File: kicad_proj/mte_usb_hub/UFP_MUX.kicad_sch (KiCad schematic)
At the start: 9 parts

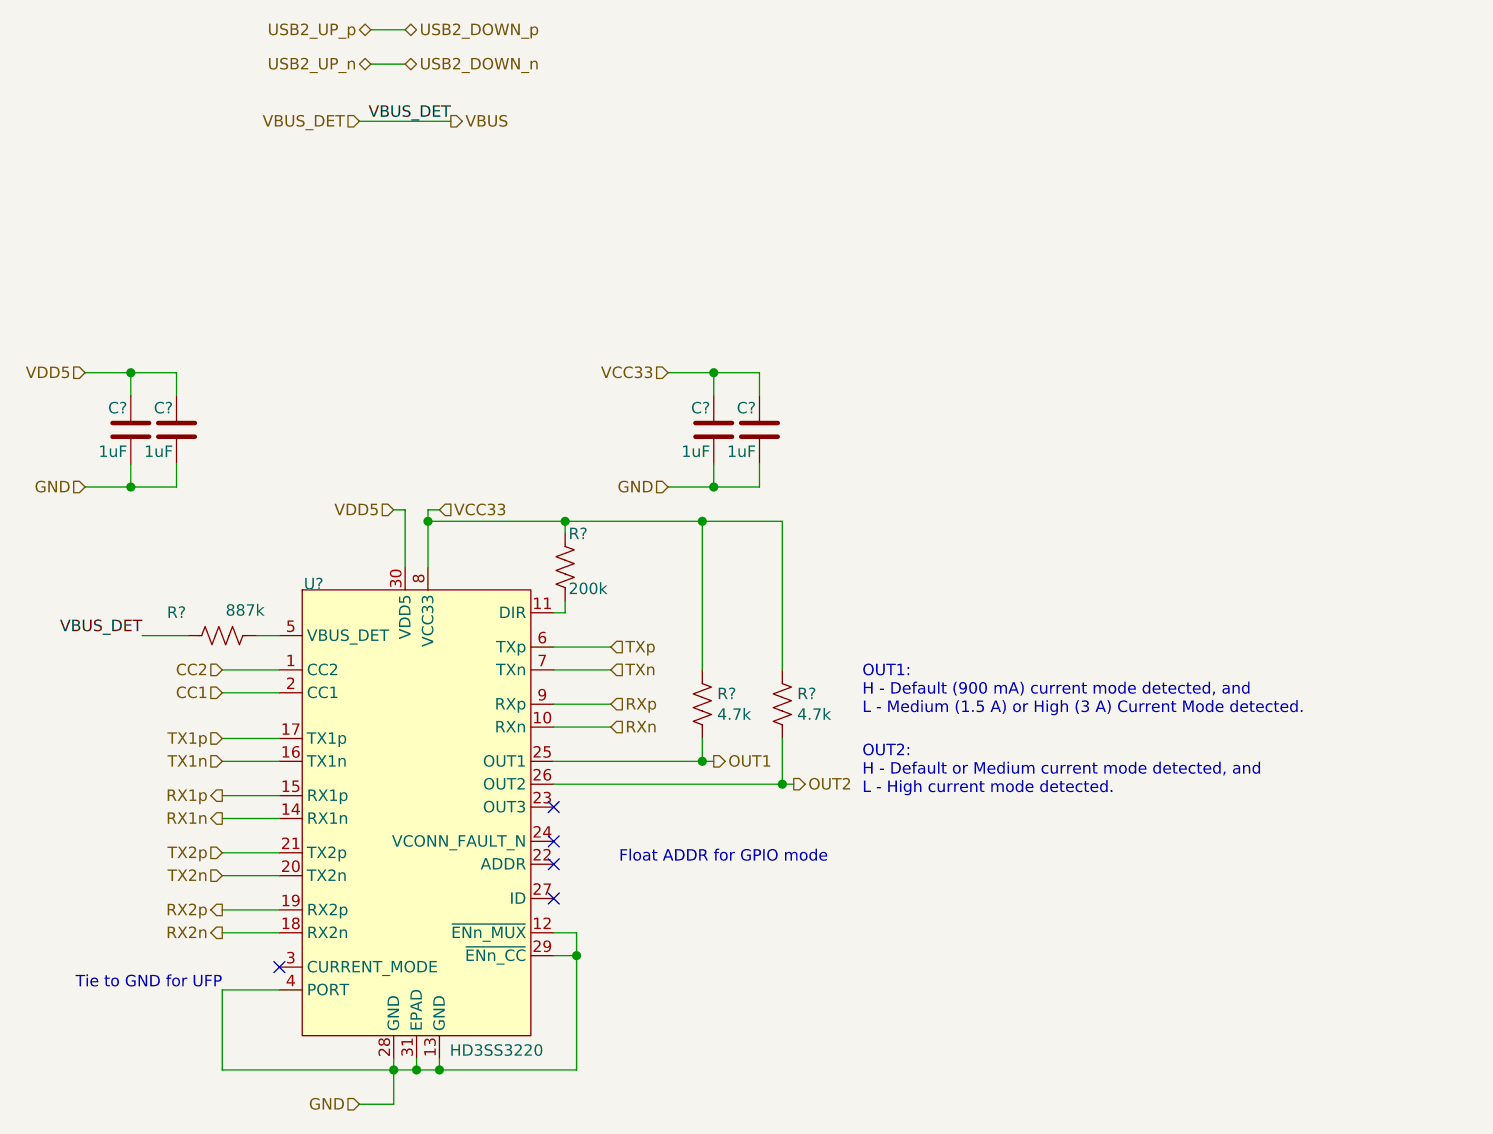
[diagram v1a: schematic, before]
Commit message: Updates input protection, output BC enabled
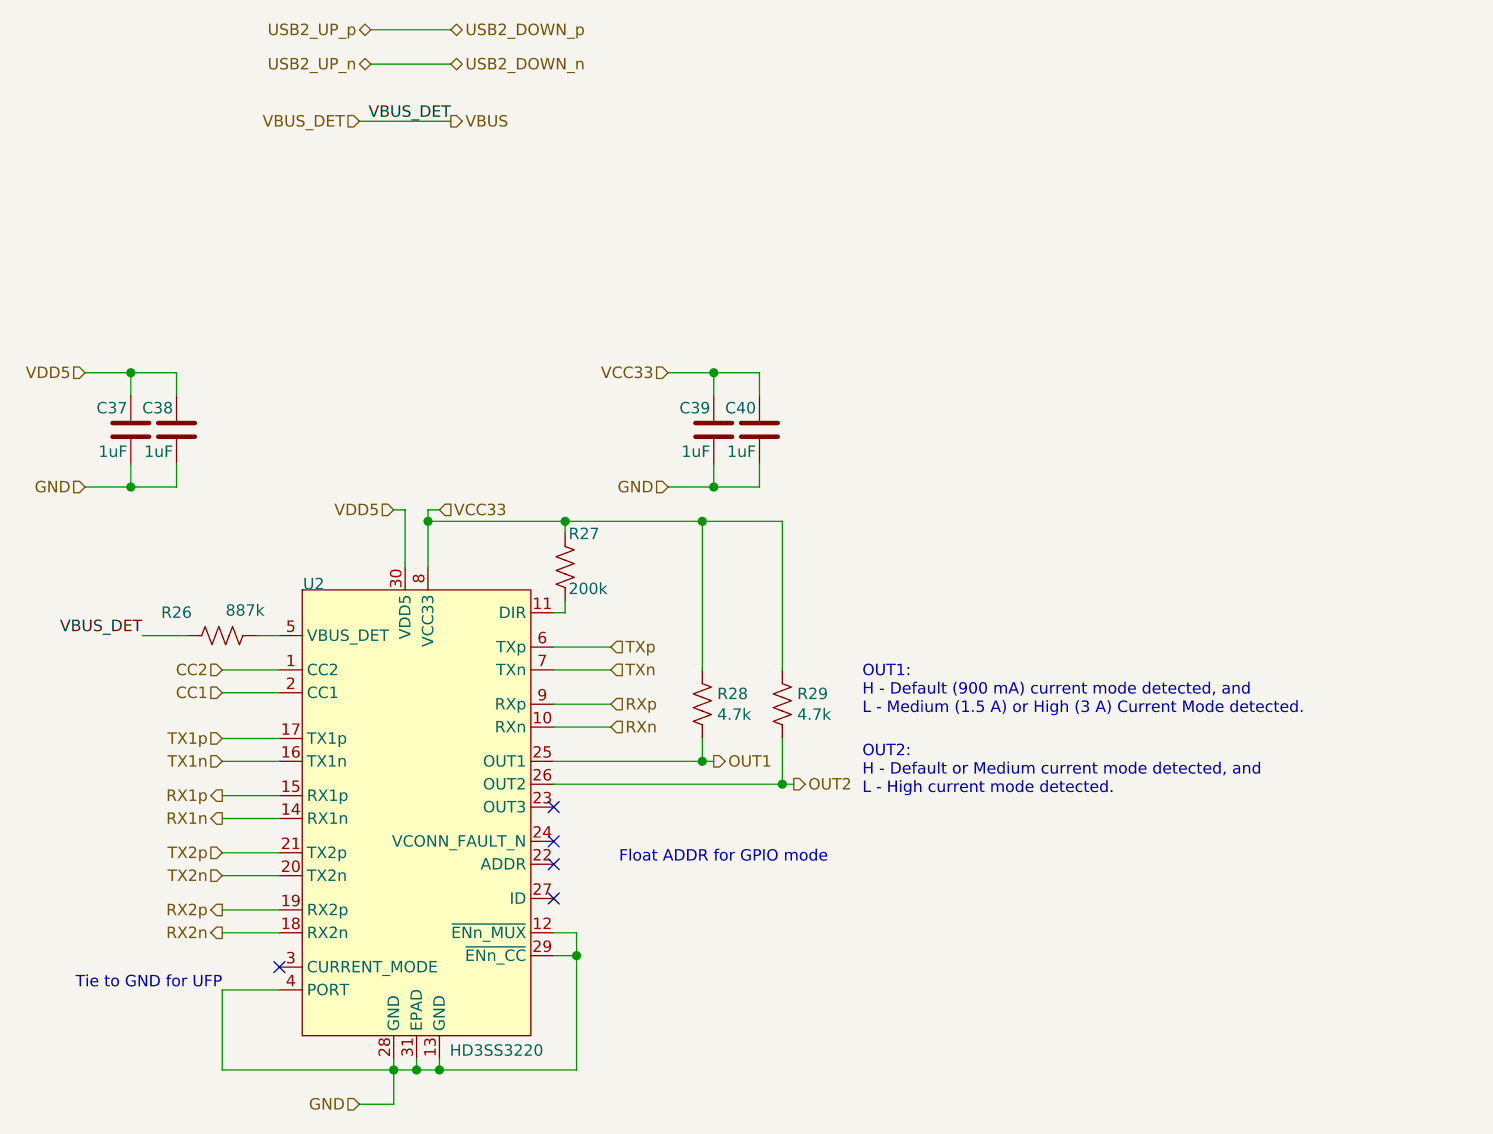
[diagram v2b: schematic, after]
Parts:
- gave numbers to parts that had none: 9
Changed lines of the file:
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@@
-(kicad_sch (version 20210126) (generator eeschema)
+(kicad_sch (version 20210406) (generator eeschema)
   (paper "A4")
   (junction (at 60.96 58.42) (diameter 1.016) (color 0 0 0 0))
@@
     (stroke (width 0) (type solid) (color 0 0 0 0))
   )
-  (wire (pts (xy 87.63 20.32) (xy 91.44 20.32))
-    (stroke (width 0) (type solid) (color 0 0 0 0))
-  )
-  (wire (pts (xy 87.63 24.13) (xy 91.44 24.13))
+  (wire (pts (xy 87.63 20.32) (xy 96.52 20.32))
+    (stroke (width 0) (type solid) (color 0 0 0 0))
+  )
+  (wire (pts (xy 87.63 24.13) (xy 96.52 24.13))
     (stroke (width 0) (type solid) (color 0 0 0 0))
   )
@@
     (effects (font (size 1.27 1.27)) (justify right))
   )
-  (hierarchical_label "USB2_DOWN_p" (shape bidirectional) (at 91.44 20.32 0)
-    (effects (font (size 1.27 1.27)) (justify left))
-  )
-  (hierarchical_label "USB2_DOWN_n" (shape bidirectional) (at 91.44 24.13 0)
-    (effects (font (size 1.27 1.27)) (justify left))
-  )
   (hierarchical_label "VCC33" (shape input) (at 95.25 73.66 0)
     (effects (font (size 1.27 1.27)) (justify left))
   )
+  (hierarchical_label "USB2_DOWN_p" (shape bidirectional) (at 96.52 20.32 0)
+    (effects (font (size 1.27 1.27)) (justify left))
+  )
+  (hierarchical_label "USB2_DOWN_n" (shape bidirectional) (at 96.52 24.13 0)
+    (effects (font (size 1.27 1.27)) (justify left))
+  )
   (hierarchical_label "VBUS" (shape output) (at 96.52 30.48 0)
     (effects (font (size 1.27 1.27)) (justify left))
@@
   (symbol (lib_id "mte_usb_hub:RC0402FR-07887KL") (at 71.12 87.63 90) (unit 1)
     (in_bom yes) (on_board yes)
-    (property "Reference" "R?" (id 0) (at 66.04 85.0708 90))
+    (property "Reference" "R26" (id 0) (at 66.04 85.0708 90))
     (property "Value" "RC0402FR-07887KL" (id 1) (at 71.12 90.17 90)
       (effects (font (size 1.27 1.27)) hide)
@@
   (symbol (lib_id "mte_usb_hub:RC0402JR-07200KL") (at 109.22 80.01 0) (unit 1)
     (in_bom yes) (on_board yes)
-    (property "Reference" "R?" (id 0) (at 109.6011 76.3206 0)
+    (property "Reference" "R27" (id 0) (at 109.6011 76.3206 0)
       (effects (font (size 1.27 1.27)) (justify left))
     )
@@
   (symbol (lib_id "mte_usb_hub:RC0402JR-074K7L") (at 124.46 95.25 0) (unit 1)
     (in_bom yes) (on_board yes)
-    (property "Reference" "R?" (id 0) (at 126.1111 94.1006 0)
+    (property "Reference" "R28" (id 0) (at 126.1111 94.1006 0)
       (effects (font (size 1.27 1.27)) (justify left))
     )
@@
   (symbol (lib_id "mte_usb_hub:RC0402JR-074K7L") (at 133.35 95.25 0) (unit 1)
     (in_bom yes) (on_board yes)
-    (property "Reference" "R?" (id 0) (at 135.0011 94.1006 0)
+    (property "Reference" "R29" (id 0) (at 135.0011 94.1006 0)
       (effects (font (size 1.27 1.27)) (justify left))
     )
@@
   (symbol (lib_id "mte_usb_hub:CC0402KRX5R7BB105") (at 60.96 64.77 0) (mirror y) (unit 1)
     (in_bom yes) (on_board yes)
-    (property "Reference" "C?" (id 0) (at 60.5789 62.3506 0)
+    (property "Reference" "C37" (id 0) (at 60.5789 62.3506 0)
       (effects (font (size 1.27 1.27)) (justify left))
     )
@@
   (symbol (lib_id "mte_usb_hub:CC0402KRX5R7BB105") (at 66.04 64.77 0) (mirror y) (unit 1)
     (in_bom yes) (on_board yes)
-    (property "Reference" "C?" (id 0) (at 65.6589 62.3506 0)
+    (property "Reference" "C38" (id 0) (at 65.6589 62.3506 0)
       (effects (font (size 1.27 1.27)) (justify left))
     )
@@
   (symbol (lib_id "mte_usb_hub:CC0402KRX5R7BB105") (at 125.73 64.77 0) (mirror y) (unit 1)
     (in_bom yes) (on_board yes)
-    (property "Reference" "C?" (id 0) (at 125.3489 62.3506 0)
+    (property "Reference" "C39" (id 0) (at 125.3489 62.3506 0)
       (effects (font (size 1.27 1.27)) (justify left))
     )
@@
   (symbol (lib_id "mte_usb_hub:CC0402KRX5R7BB105") (at 130.81 64.77 0) (mirror y) (unit 1)
     (in_bom yes) (on_board yes)
-    (property "Reference" "C?" (id 0) (at 130.4289 62.3506 0)
+    (property "Reference" "C40" (id 0) (at 130.4289 62.3506 0)
       (effects (font (size 1.27 1.27)) (justify left))
     )
@@
   (symbol (lib_id "mte_usb_hub:HD3SS3220") (at 92.71 107.95 0) (unit 1)
     (in_bom yes) (on_board yes)
-    (property "Reference" "U?" (id 0) (at 81.28 81.8958 0))
+    (property "Reference" "U2" (id 0) (at 81.28 81.8958 0))
     (property "Value" "HD3SS3220" (id 1) (at 101.6 133.7245 0))
     (property "Footprint" "" (id 2) (at 92.71 95.25 0)

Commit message: New changes from the livestream
Starts the layout
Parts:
- C37, C38, C39, C40: footprint footprints:CAPACITOR_0402N -> mte_usb_footprints:CAPACITOR_0402N
- R26, R27, R28, R29: footprint footprints:RESISTOR_0402N -> mte_usb_footprints:RESISTOR_0402N
- U2: footprint (none) -> mte_usb_footprints:QFN31P40_250X450X80L30X20T120X320N
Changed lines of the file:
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@@
       (effects (font (size 1.27 1.27)) hide)
     )
-    (property "Footprint" "footprints:RESISTOR_0402N" (id 2) (at 71.374 86.614 90)
+    (property "Footprint" "mte_usb_footprints:RESISTOR_0402N" (id 2) (at 71.374 86.614 90)
       (effects (font (size 1.27 1.27)) hide)
     )
@@
       (effects (font (size 1.27 1.27)) hide)
     )
-    (property "Footprint" "footprints:RESISTOR_0402N" (id 2) (at 110.236 80.264 90)
+    (property "Footprint" "mte_usb_footprints:RESISTOR_0402N" (id 2) (at 110.236 80.264 90)
       (effects (font (size 1.27 1.27)) hide)
     )
@@
       (effects (font (size 1.27 1.27)) hide)
     )
-    (property "Footprint" "footprints:RESISTOR_0402N" (id 2) (at 125.476 95.504 90)
+    (property "Footprint" "mte_usb_footprints:RESISTOR_0402N" (id 2) (at 125.476 95.504 90)
       (effects (font (size 1.27 1.27)) hide)
     )
@@
       (effects (font (size 1.27 1.27)) hide)
     )
-    (property "Footprint" "footprints:RESISTOR_0402N" (id 2) (at 134.366 95.504 90)
+    (property "Footprint" "mte_usb_footprints:RESISTOR_0402N" (id 2) (at 134.366 95.504 90)
       (effects (font (size 1.27 1.27)) hide)
     )
@@
       (effects (font (size 1.27 1.27)) (justify left) hide)
     )
-    (property "Footprint" "footprints:CAPACITOR_0402N" (id 2) (at 59.9948 68.58 0)
+    (property "Footprint" "mte_usb_footprints:CAPACITOR_0402N" (id 2) (at 59.9948 68.58 0)
       (effects (font (size 1.27 1.27)) hide)
     )
@@
       (effects (font (size 1.27 1.27)) (justify left) hide)
     )
-    (property "Footprint" "footprints:CAPACITOR_0402N" (id 2) (at 65.0748 68.58 0)
+    (property "Footprint" "mte_usb_footprints:CAPACITOR_0402N" (id 2) (at 65.0748 68.58 0)
       (effects (font (size 1.27 1.27)) hide)
     )
@@
       (effects (font (size 1.27 1.27)) (justify left) hide)
     )
-    (property "Footprint" "footprints:CAPACITOR_0402N" (id 2) (at 124.7648 68.58 0)
+    (property "Footprint" "mte_usb_footprints:CAPACITOR_0402N" (id 2) (at 124.7648 68.58 0)
       (effects (font (size 1.27 1.27)) hide)
     )
@@
       (effects (font (size 1.27 1.27)) (justify left) hide)
     )
-    (property "Footprint" "footprints:CAPACITOR_0402N" (id 2) (at 129.8448 68.58 0)
+    (property "Footprint" "mte_usb_footprints:CAPACITOR_0402N" (id 2) (at 129.8448 68.58 0)
       (effects (font (size 1.27 1.27)) hide)
     )
@@
     (property "Reference" "U2" (id 0) (at 81.28 81.8958 0))
     (property "Value" "HD3SS3220" (id 1) (at 101.6 133.7245 0))
-    (property "Footprint" "" (id 2) (at 92.71 95.25 0)
+    (property "Footprint" "mte_usb_footprints:QFN31P40_250X450X80L30X20T120X320N" (id 2) (at 92.71 95.25 0)
       (effects (font (size 1.27 1.27)) hide)
     )

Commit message: Updates from the livestream
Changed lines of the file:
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@@
-(kicad_sch (version 20210406) (generator eeschema)
+(kicad_sch (version 20210606) (generator eeschema)
   (paper "A4")
   (junction (at 60.96 58.42) (diameter 1.016) (color 0 0 0 0))
